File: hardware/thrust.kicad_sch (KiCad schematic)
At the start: 18 parts, among them J13 KNOB (VH/W/VL), J14 CONTACTOR 12V, Q2 IRLZ44N, U2 74AHCT125, U3 X9C103, U4 MCP6002-I/P

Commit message: feat: MPN table merged into schematic fields; SES import script
Co-Authored-By: Claude Fable 5 <noreply@anthropic.com>
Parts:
- D7: MPN (none) -> 1N4007
- J13: MPN (none) -> CUI TB007-508-03
- J14: MPN (none) -> CUI TB007-508-02
- Q2: MPN (none) -> IRLZ44NPBF
- U2: MPN (none) -> SN74AHCT125N
- U3: MPN (none) -> X9C103P
- U4: MPN (none) -> MCP6002-I/P
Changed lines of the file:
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@@
     (property "Datasheet" "" (at 69.85 100.33 0)
+      (effects (font (size 1.27 1.27)) (hide yes)))
+    (property "MPN" "SN74AHCT125N" (at 69.85 100.33 0)
       (effects (font (size 1.27 1.27)) (hide yes)))
     (pin "1")
@@
     (property "Datasheet" "" (at 139.7 100.33 0)
       (effects (font (size 1.27 1.27)) (hide yes)))
+    (property "MPN" "X9C103P" (at 139.7 100.33 0)
+      (effects (font (size 1.27 1.27)) (hide yes)))
     (pin "1")
     (pin "2")
@@
     (property "Datasheet" "" (at 209.55 100.33 0)
       (effects (font (size 1.27 1.27)) (hide yes)))
+    (property "MPN" "MCP6002-I/P" (at 209.55 100.33 0)
+      (effects (font (size 1.27 1.27)) (hide yes)))
     (pin "1")
     (pin "2")
@@
     (property "Datasheet" "" (at 340.36 100.33 0)
       (effects (font (size 1.27 1.27)) (hide yes)))
+    (property "MPN" "CUI TB007-508-03" (at 340.36 100.33 0)
+      (effects (font (size 1.27 1.27)) (hide yes)))
     (pin "1")
     (pin "2")
@@
     (property "Datasheet" "" (at 139.7 160.02 0)
       (effects (font (size 1.27 1.27)) (hide yes)))
+    (property "MPN" "IRLZ44NPBF" (at 139.7 160.02 0)
+      (effects (font (size 1.27 1.27)) (hide yes)))
     (pin "1")
     (pin "2")
@@
     (property "Datasheet" "" (at 82.55 214.63 0)
       (effects (font (size 1.27 1.27)) (hide yes)))
+    (property "MPN" "1N4007" (at 82.55 214.63 0)
+      (effects (font (size 1.27 1.27)) (hide yes)))
     (pin "1")
     (pin "2")
@@
     (property "Datasheet" "" (at 209.55 160.02 0)
       (effects (font (size 1.27 1.27)) (hide yes)))
-    (pin "1")
+    (property "MPN" "CUI TB007-508-02" (at 209.55 160.02 0)
+      (effects (font (size 1.27 1.27)) (hide yes)))
+    (pin "1")

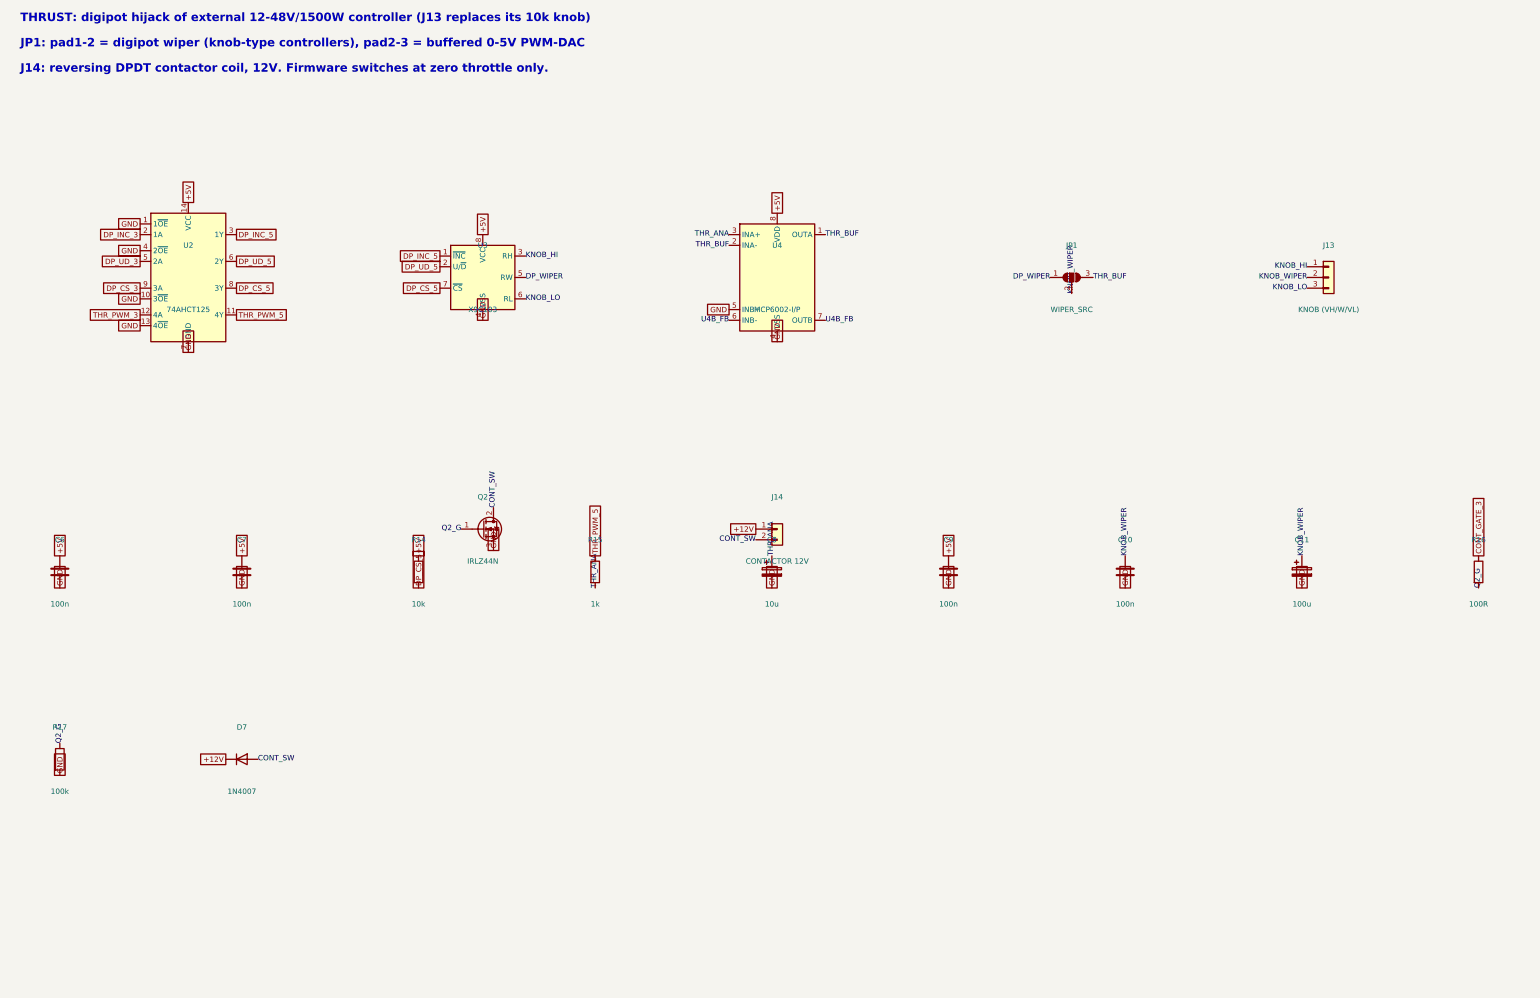
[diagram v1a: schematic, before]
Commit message: feat: on-board 800W H-bridge (HIP4082 + 8 FET, ACS758, M5 lugs) + BTN8982 servo bridge; 160x120 board, placement DRC-clean
Co-Authored-By: Claude Fable 5 <noreply@anthropic.com>
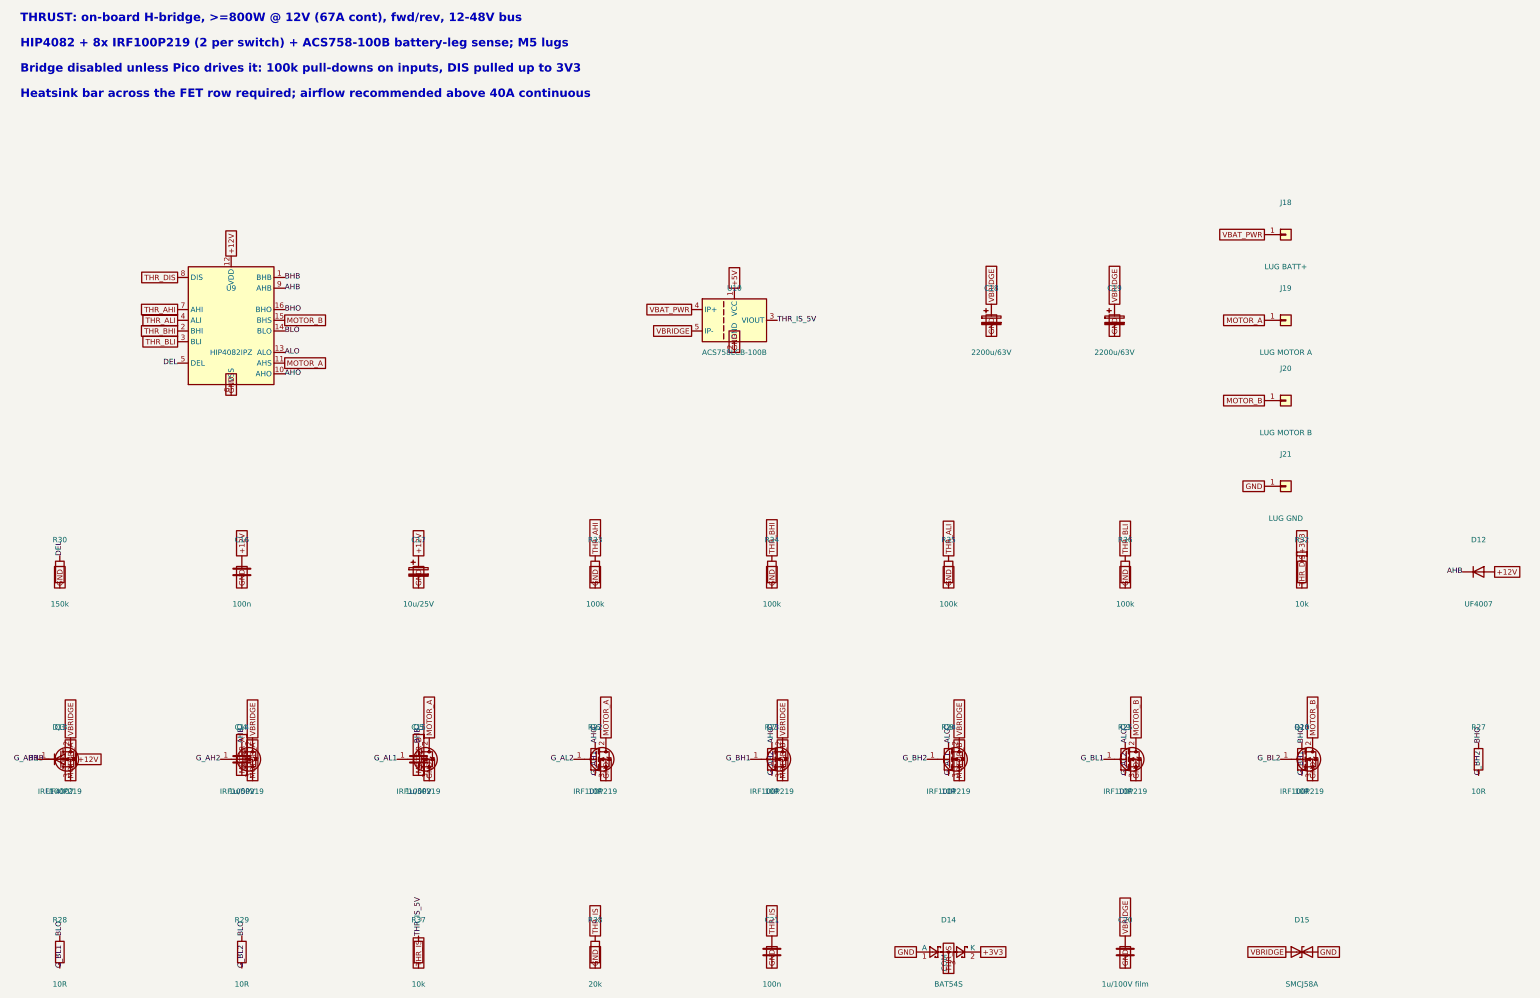
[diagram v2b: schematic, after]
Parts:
- removed C10, C6, C7, C9: 100n, Capacitor_THT:C_Disc_D5.0mm_W2.5mm_P5.00mm, symbol Device:C
- removed C11: 100u, Capacitor_THT:CP_Radial_D5.0mm_P2.00mm, symbol Device:C_Polarized
- removed C8: 10u, Capacitor_THT:CP_Radial_D5.0mm_P2.00mm, symbol Device:C_Polarized
- removed D7: 1N4007, Diode_THT:D_DO-41_SOD81_P10.16mm_Horizontal, symbol Diode:1N4007
- removed J13: KNOB (VH/W/VL), TerminalBlock_CUI:TerminalBlock_CUI_TB007-508-03_1x03_P5.08mm_Horizontal, symbol Connector_Generic:Conn_01x03
- removed J14: CONTACTOR 12V, TerminalBlock_CUI:TerminalBlock_CUI_TB007-508-02_1x02_P5.08mm_Horizontal, symbol Connector_Generic:Conn_01x02
- removed JP1: WIPER_SRC, Jumper:SolderJumper-3_P1.3mm_Open_RoundedPad1.0x1.5mm, symbol Jumper:SolderJumper_3_Open
- removed Q2: IRLZ44N, Package_TO_SOT_THT:TO-220-3_Vertical, symbol Transistor_FET:IRLZ44N
- removed R14: 10k, Resistor_THT:R_Axial_DIN0207_L6.3mm_D2.5mm_P10.16mm_Horizontal, symbol Device:R
- removed R15: 1k, Resistor_THT:R_Axial_DIN0207_L6.3mm_D2.5mm_P10.16mm_Horizontal, symbol Device:R
- removed R16: 100R, Resistor_THT:R_Axial_DIN0207_L6.3mm_D2.5mm_P10.16mm_Horizontal, symbol Device:R
- removed R17: 100k, Resistor_THT:R_Axial_DIN0207_L6.3mm_D2.5mm_P10.16mm_Horizontal, symbol Device:R
- removed U2: 74AHCT125, Package_DIP:DIP-14_W7.62mm_Socket, symbol vanchor-helm:74AHCT125_flat
- removed U3: X9C103, Package_DIP:DIP-8_W7.62mm_Socket, symbol vanchor-helm:X9C103
- removed U4: MCP6002-I/P, Package_DIP:DIP-8_W7.62mm_Socket, symbol vanchor-helm:MCP6002_flat
- added C14, C15: 1u/50V, Capacitor_THT:C_Disc_D5.0mm_W2.5mm_P5.00mm, symbol Device:C
- added C16, C21: 100n, Capacitor_THT:C_Disc_D5.0mm_W2.5mm_P5.00mm, symbol Device:C
- added C17: 10u/25V, Capacitor_THT:CP_Radial_D5.0mm_P2.00mm, symbol Device:C_Polarized
- added C18, C19: 2200u/63V, Capacitor_THT:CP_Radial_D18.0mm_P7.50mm, symbol Device:C_Polarized
- added C20: 1u/100V film, Capacitor_THT:C_Disc_D5.0mm_W2.5mm_P5.00mm, symbol Device:C
- added D12, D13: UF4007, Diode_THT:D_DO-41_SOD81_P10.16mm_Horizontal, symbol Diode:1N4007
- added D14: BAT54S, Package_TO_SOT_SMD:SOT-23, symbol Diode:BAT54S
- added D15: SMCJ58A, Diode_SMD:D_SMC, symbol Device:D_TVS
- added J18: LUG BATT+, vanchor-helm:Lug_M5, symbol Connector_Generic:Conn_01x01
- added J19: LUG MOTOR A, vanchor-helm:Lug_M5, symbol Connector_Generic:Conn_01x01
- added J20: LUG MOTOR B, vanchor-helm:Lug_M5, symbol Connector_Generic:Conn_01x01
- added J21: LUG GND, vanchor-helm:Lug_M5, symbol Connector_Generic:Conn_01x01
- added Q10, Q3, Q4, Q5, Q6, Q7, Q8, Q9: IRF100P219, Package_TO_SOT_THT:TO-220-3_Vertical, symbol Transistor_FET:IRLZ44N
- added R22, R23, R24, R25, R26, R27, R28, R29: 10R, Resistor_THT:R_Axial_DIN0207_L6.3mm_D2.5mm_P10.16mm_Horizontal, symbol Device:R
- added R30: 150k, Resistor_THT:R_Axial_DIN0207_L6.3mm_D2.5mm_P10.16mm_Horizontal, symbol Device:R
- added R32, R37: 10k, Resistor_THT:R_Axial_DIN0207_L6.3mm_D2.5mm_P10.16mm_Horizontal, symbol Device:R
- added R33, R34, R35, R36: 100k, Resistor_THT:R_Axial_DIN0207_L6.3mm_D2.5mm_P10.16mm_Horizontal, symbol Device:R
- added R38: 20k, Resistor_THT:R_Axial_DIN0207_L6.3mm_D2.5mm_P10.16mm_Horizontal, symbol Device:R
- added U10: ACS758LCB-100B, Sensor_Current:Allegro_CB_PFF, symbol Sensor_Current:ACS758xCB-100B-PFF
- added U9: HIP4082IPZ, Package_DIP:DIP-16_W7.62mm_Socket, symbol Driver_FET:HIP4082xP
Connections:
- net +12V: now also C16.1, C17.1, D12.2 (A), D13.2 (A), U9.12 (VDD)
- net +5V: now also U10.1 (VCC)
- net GND: now also C16.2, C17.2, C18.2, C19.2, C20.2, C21.2, D14.1 (A), D15.2 (A2), J21.1 (Pin_1), Q10.3 (S), Q5.3 (S), Q6.3 (S), Q9.3 (S), R30.2, R33.2, R34.2, R35.2, R36.2, R38.2, U10.2 (GND), U9.6 (VSS)
- new net +3V3: D14.2 (K), R32.1
- new net AHB: C14.1, D12.1 (K), U9.9 (AHB)
- new net AHO: R22.1, R23.1, U9.10 (AHO)
- new net ALO: R24.1, R25.1, U9.13 (ALO)
- new net BHB: C15.1, D13.1 (K), U9.1 (BHB)
- new net BHO: R26.1, R27.1, U9.16 (BHO)
- new net BLO: R28.1, R29.1, U9.14 (BLO)
- new net DEL: R30.1, U9.5 (DEL)
- new net G_AH1: Q3.1 (G), R22.2
- new net G_AH2: Q4.1 (G), R23.2
- new net G_AL1: Q5.1 (G), R24.2
- new net G_AL2: Q6.1 (G), R25.2
- new net G_BH1: Q7.1 (G), R26.2
- new net G_BH2: Q8.1 (G), R27.2
- new net G_BL1: Q9.1 (G), R28.2
- new net G_BL2: Q10.1 (G), R29.2
- new net MOTOR_A: C14.2, J19.1 (Pin_1), Q3.3 (S), Q4.3 (S), Q5.2 (D), Q6.2 (D), U9.11 (AHS)
- new net MOTOR_B: C15.2, J20.1 (Pin_1), Q10.2 (D), Q7.3 (S), Q8.3 (S), Q9.2 (D), U9.15 (BHS)
- new net THR_AHI: R33.1, U9.7 (AHI)
- new net THR_ALI: R35.1, U9.4 (ALI)
- new net THR_BHI: R34.1, U9.2 (BHI)
- new net THR_BLI: R36.1, U9.3 (BLI)
- new net THR_DIS: R32.2, U9.8 (DIS)
- new net THR_IS: C21.1, D14.3 (COM), R37.2, R38.1
- new net THR_IS_5V: R37.1, U10.3 (VIOUT)
- new net VBAT_PWR: J18.1 (Pin_1), U10.4 (IP+)
- new net VBRIDGE: C18.1, C19.1, C20.1, D15.1 (A1), Q3.2 (D), Q4.2 (D), Q7.2 (D), Q8.2 (D), U10.5 (IP-)
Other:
- note added: "Bridge disabled unless Pico drives it: 100k pull-downs on inputs, DIS pulled up to 3V3"
- note added: "HIP4082 + 8x IRF100P219 (2 per switch) + ACS758-100B battery-leg sense; M5 lugs"
- note added: "Heatsink bar across the FET row required; airflow recommended above 40A continuous"
- note added: "THRUST: on-board H-bridge, >=800W @ 12V (67A cont), fwd/rev, 12-48V bus"
- note removed: "J14: reversing DPDT contactor coil, 12V. Firmware switches at zero throttle only."
- note removed: "JP1: pad1-2 = digipot wiper (knob-type controllers), pad2-3 = buffered 0-5V PWM-DAC"
- note removed: "THRUST: digipot hijack of external 12-48V/1500W controller (J13 replaces its 10k knob)"

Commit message: feat: routed board via scripted freerouting pipeline (T10) — known GUI touch-up items documented
Co-Authored-By: Claude Fable 5 <noreply@anthropic.com>
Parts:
- R22, R23, R24, R25, R26, R27, R28, R29: footprint Resistor_THT:R_Axial_DIN0207_L6.3mm_D2.5mm_P10.16mm_Horizontal -> Resistor_THT:R_Axial_DIN0207_L6.3mm_D2.5mm_P2.54mm_Vertical
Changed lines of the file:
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@@
     (property "Value" "10R" (at 166.37 222.25 0)
       (effects (font (size 1.27 1.27))))
-    (property "Footprint" "Resistor_THT:R_Axial_DIN0207_L6.3mm_D2.5mm_P10.16mm_Horizontal" (at 166.37 214.63 0)
+    (property "Footprint" "Resistor_THT:R_Axial_DIN0207_L6.3mm_D2.5mm_P2.54mm_Vertical" (at 166.37 214.63 0)
       (effects (font (size 1.27 1.27)) (hide yes)))
     (property "Datasheet" "" (at 166.37 214.63 0)
@@
     (property "Value" "10R" (at 208.28 222.25 0)
       (effects (font (size 1.27 1.27))))
-    (property "Footprint" "Resistor_THT:R_Axial_DIN0207_L6.3mm_D2.5mm_P10.16mm_Horizontal" (at 208.28 214.63 0)
+    (property "Footprint" "Resistor_THT:R_Axial_DIN0207_L6.3mm_D2.5mm_P2.54mm_Vertical" (at 208.28 214.63 0)
       (effects (font (size 1.27 1.27)) (hide yes)))
     (property "Datasheet" "" (at 208.28 214.63 0)
@@
     (property "Value" "10R" (at 250.19 222.25 0)
       (effects (font (size 1.27 1.27))))
-    (property "Footprint" "Resistor_THT:R_Axial_DIN0207_L6.3mm_D2.5mm_P10.16mm_Horizontal" (at 250.19 214.63 0)
+    (property "Footprint" "Resistor_THT:R_Axial_DIN0207_L6.3mm_D2.5mm_P2.54mm_Vertical" (at 250.19 214.63 0)
       (effects (font (size 1.27 1.27)) (hide yes)))
     (property "Datasheet" "" (at 250.19 214.63 0)
@@
     (property "Value" "10R" (at 292.1 222.25 0)
       (effects (font (size 1.27 1.27))))
-    (property "Footprint" "Resistor_THT:R_Axial_DIN0207_L6.3mm_D2.5mm_P10.16mm_Horizontal" (at 292.1 214.63 0)
+    (property "Footprint" "Resistor_THT:R_Axial_DIN0207_L6.3mm_D2.5mm_P2.54mm_Vertical" (at 292.1 214.63 0)
       (effects (font (size 1.27 1.27)) (hide yes)))
     (property "Datasheet" "" (at 292.1 214.63 0)
@@
     (property "Value" "10R" (at 334.01 222.25 0)
       (effects (font (size 1.27 1.27))))
-    (property "Footprint" "Resistor_THT:R_Axial_DIN0207_L6.3mm_D2.5mm_P10.16mm_Horizontal" (at 334.01 214.63 0)
+    (property "Footprint" "Resistor_THT:R_Axial_DIN0207_L6.3mm_D2.5mm_P2.54mm_Vertical" (at 334.01 214.63 0)
       (effects (font (size 1.27 1.27)) (hide yes)))
     (property "Datasheet" "" (at 334.01 214.63 0)
@@
     (property "Value" "10R" (at 375.92 222.25 0)
       (effects (font (size 1.27 1.27))))
-    (property "Footprint" "Resistor_THT:R_Axial_DIN0207_L6.3mm_D2.5mm_P10.16mm_Horizontal" (at 375.92 214.63 0)
+    (property "Footprint" "Resistor_THT:R_Axial_DIN0207_L6.3mm_D2.5mm_P2.54mm_Vertical" (at 375.92 214.63 0)
       (effects (font (size 1.27 1.27)) (hide yes)))
     (property "Datasheet" "" (at 375.92 214.63 0)
@@
     (property "Value" "10R" (at 39.37 267.97 0)
       (effects (font (size 1.27 1.27))))
-    (property "Footprint" "Resistor_THT:R_Axial_DIN0207_L6.3mm_D2.5mm_P10.16mm_Horizontal" (at 39.37 260.35 0)
+    (property "Footprint" "Resistor_THT:R_Axial_DIN0207_L6.3mm_D2.5mm_P2.54mm_Vertical" (at 39.37 260.35 0)
       (effects (font (size 1.27 1.27)) (hide yes)))
     (property "Datasheet" "" (at 39.37 260.35 0)
@@
     (property "Value" "10R" (at 82.55 267.97 0)
       (effects (font (size 1.27 1.27))))
-    (property "Footprint" "Resistor_THT:R_Axial_DIN0207_L6.3mm_D2.5mm_P10.16mm_Horizontal" (at 82.55 260.35 0)
+    (property "Footprint" "Resistor_THT:R_Axial_DIN0207_L6.3mm_D2.5mm_P2.54mm_Vertical" (at 82.55 260.35 0)
       (effects (font (size 1.27 1.27)) (hide yes)))
     (property "Datasheet" "" (at 82.55 260.35 0)
